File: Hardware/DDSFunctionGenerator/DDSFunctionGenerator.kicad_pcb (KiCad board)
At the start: 2 copper layers, 80 x 65 mm, 155 parts, among them J1 Conn_Coaxial, J2 USB_B_Micro, J3 DG128-5.0-02P-14-00A, J4 Conn_01x02_Female, J5 Conn_Coaxial, J6 Conn_Coaxial, J7 Conn_01x04_Male, J8 Conn_01x04_Female, J9 Conn_01x04_Female, Q1 Q_NPN_BEC, Q2 Q_NPN_BEC, Q3 Q_NPN_BEC, SW1 EN11-VSB1AQ15, T1 Transformer_1P_1S, U1 TC1107-3.3VOA, U2 L7805, U3 L78L33_SO8, U4 AD9832, U5 STM32F030K6Tx, U6 FT200XD, U7 AD8325, U8 MCP3425A0T-ECH, X1 XO91, Y1 20MHz

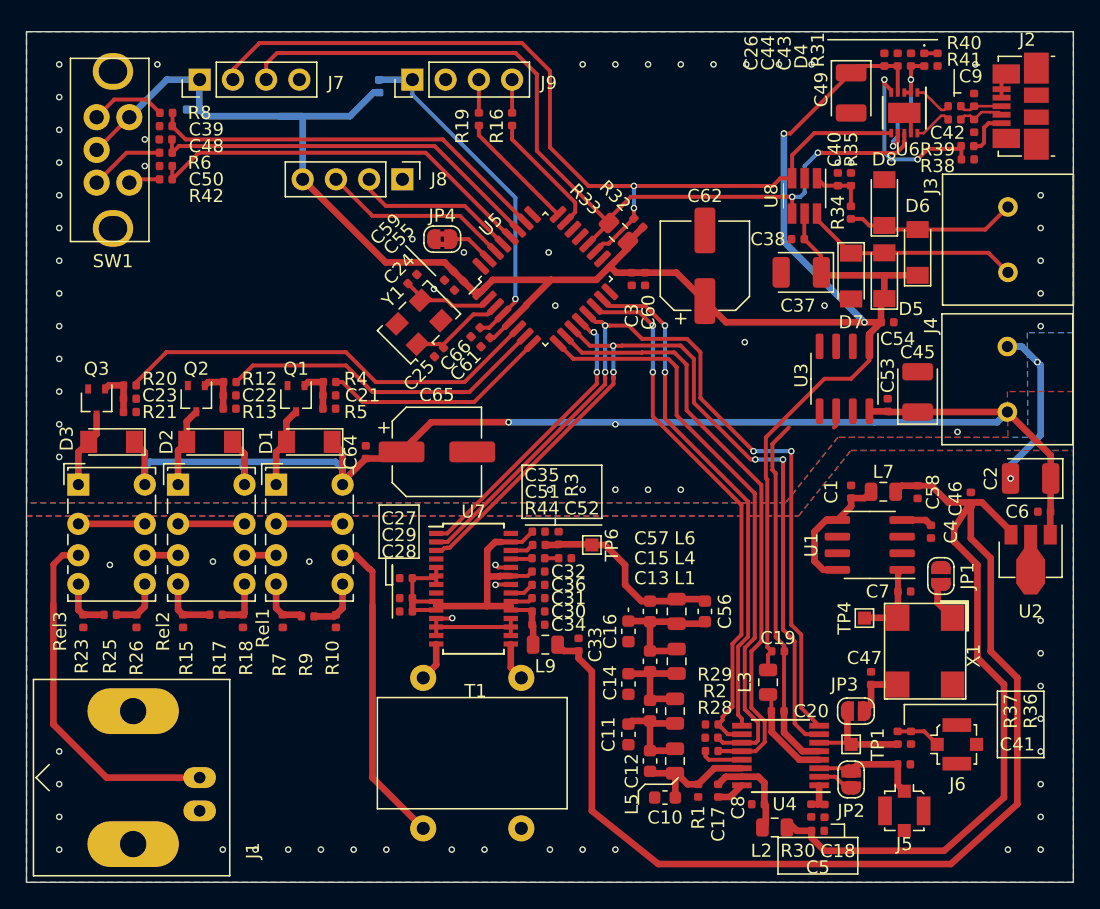
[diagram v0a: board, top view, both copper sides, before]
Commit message: fix #149, fix #150, fix #151, fix #152, fix #153, fix #154
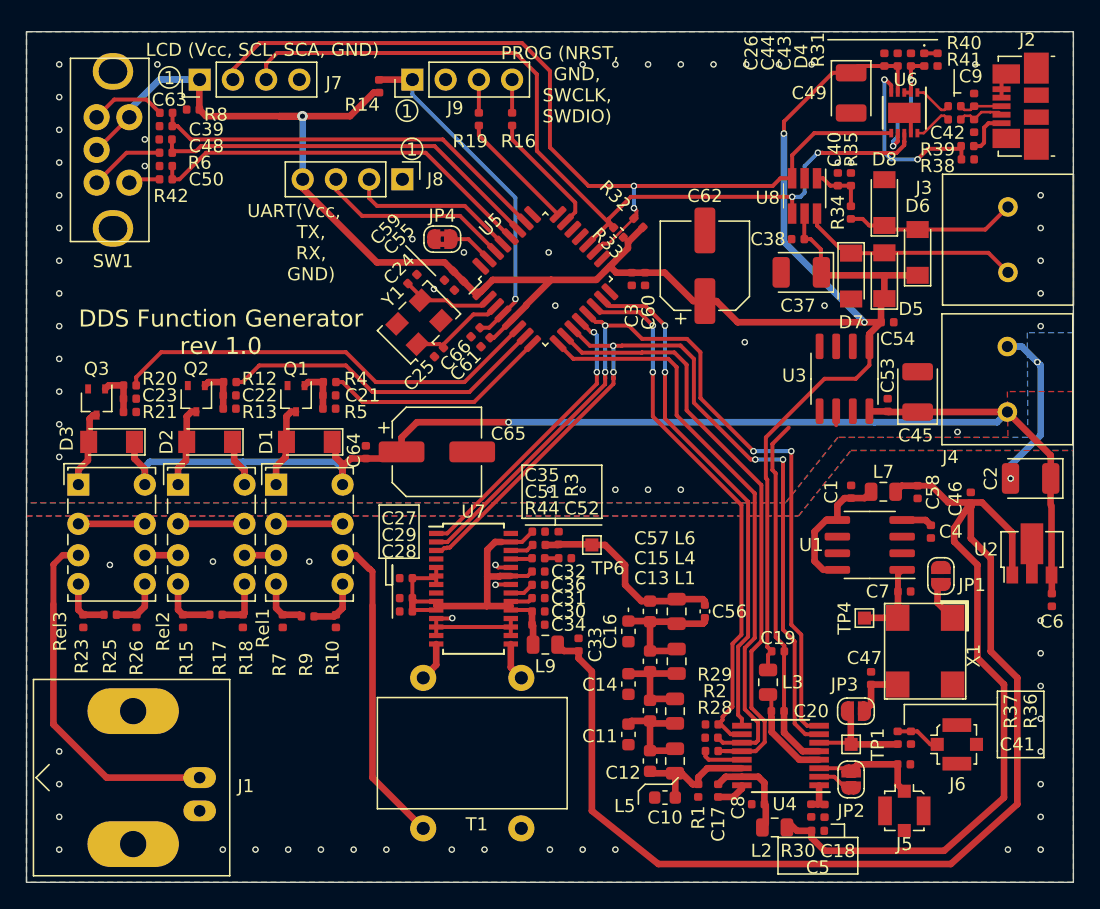
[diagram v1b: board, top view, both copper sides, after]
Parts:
- C24, C25: value 8p -> 8p2
- C56: footprint Capacitor_SMD:C_0603_1608Metric -> Capacitor_SMD:C_0402_1005Metric
- C63, R14: moved to F.Cu
- C64: value 2u2 -> 100n
- R33: footprint Resistor_SMD:R_0805_2012Metric_Pad1.15x1.40mm_HandSolder -> Resistor_SMD:R_0402_1005Metric
- U2: value L7805 -> L78L08_SOT89
- moved C6 6.77 mm to (143.4, 113.4), turned to 270 degrees
- moved U2 0.11 mm to (141.8, 109.9), turned to 90 degrees
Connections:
- U2 pad 1: 9V -> 5V_ANALOG
- U2 pad 3: 5V_ANALOG -> 9V
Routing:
- net 9V: track 106.9 -> 111.4 mm, vias 2 -> 1
- net 5V_ANALOG: track 128.9 -> 132.0 mm
- net 5V_DIGITAL: track 173.1 -> 175.4 mm, vias 2 -> 3
- net SPI1_MOSI: track 66.4 -> 66.9 mm
- net SDA: track 67.6 -> 68.1 mm
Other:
- board text added: "1"
- board text added: "DDS Function Generator rev 1.0"
- board text added: "LCD (Vcc, SCL, SCA, GND)"
- board text added: "PROG (NRST, GND, SWCLK, SWDIO)"
- board text added: "UART(Vcc, TX, RX, GND)"

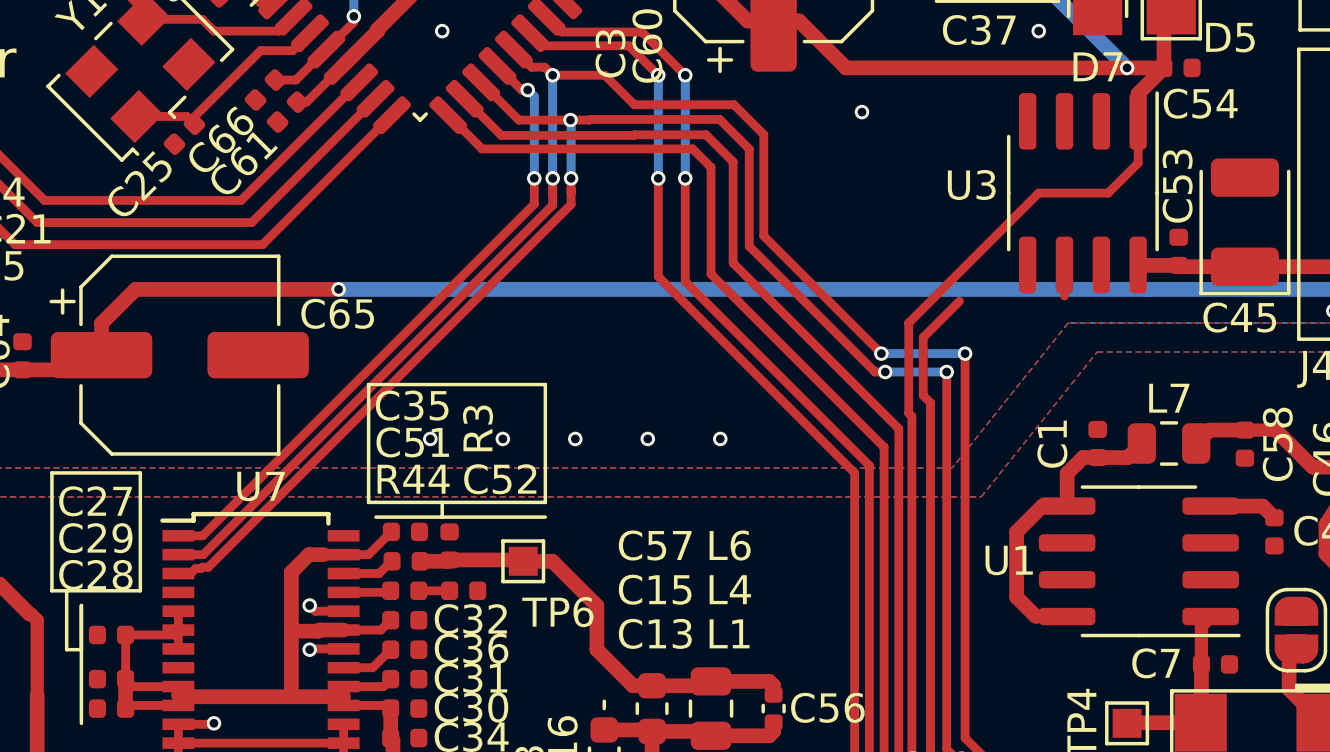
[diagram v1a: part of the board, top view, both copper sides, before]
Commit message: fix #156
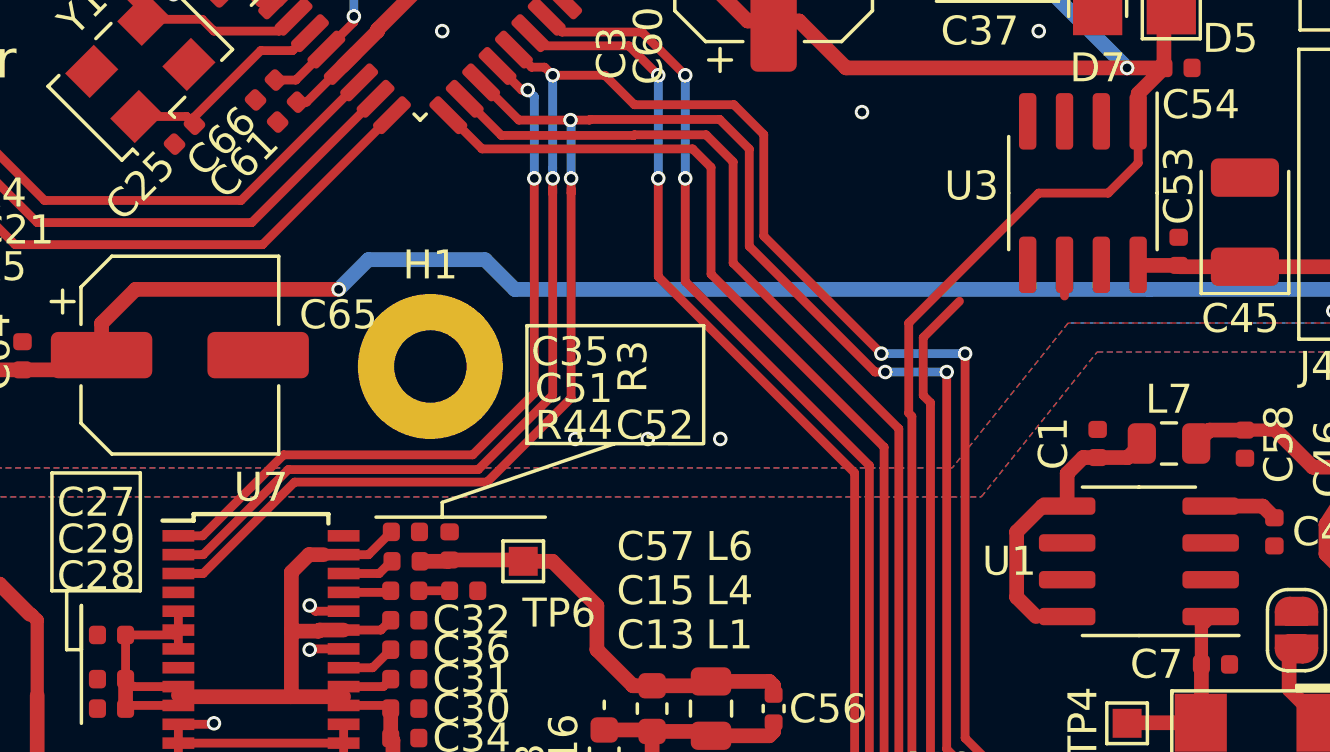
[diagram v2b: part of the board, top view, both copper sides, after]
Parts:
- added H1: MountingHole_Pad, MountingHole:MountingHole_2.5mm_Pad, F.Cu at (105.0, 102.5)
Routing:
- net SPI1_SCK: track 66.8 -> 70.7 mm
- net SPI1_MOSI: track 66.9 -> 70.7 mm
- net SPI1_CS_AMPLIFIER: track 22.8 -> 26.6 mm
- net 9V: track 111.4 -> 112.2 mm
- net GND: vias 77 -> 75

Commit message: cleanup after transition to KiCad6
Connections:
- C39 pad 1: ROT_B -> ROT_A
- R8 pad 1: ROT_B -> ROT_A
- U5 pad 26: ROT_B -> ROT_A
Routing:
- net ROT_B: track 31.0 -> 0.00 mm
- net ROT_A: track 30.3 -> 61.3 mm
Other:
- net class Default removed
- net class rf_power_supply removed
